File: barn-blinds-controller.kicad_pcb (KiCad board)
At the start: 4 copper layers, 65 x 73.9 mm, 103 parts, among them J1 DC005-T20, J2 USB_B_Micro, J3 Conn_01x05, J4 Phoenix Contact 1786918, SW1 RESET, SW2 BOOT, U1 DCDC Converter, U10 TMP235, U11 ACS723xLCTR-05AB, U12 PRTR5V0U2X, U13 PRTR5V0U2X, U14 PRTR5V0U2X, U15 PRTR5V0U2X, U2 AP2112K-3.3, U3 ESP32-S3-WROOM-1, U4 ISO7760DBQ, U5 ISO7760DBQ, U6 ISO7760DBQ, U7 AMS1117-3.3, U8 TB6612FNG, U9 TB6612FNG

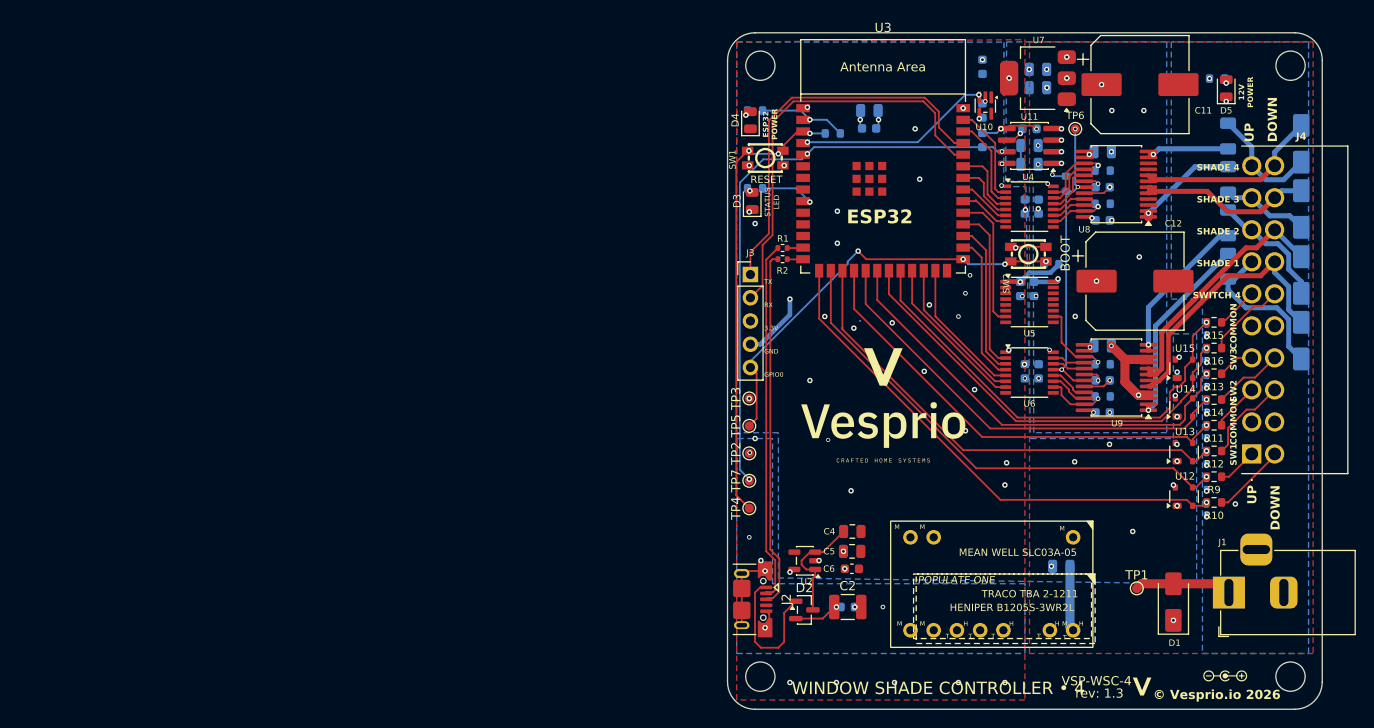
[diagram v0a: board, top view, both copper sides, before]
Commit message: Added RTS/DTS programing via UART circuitry, added LED control circuitry.
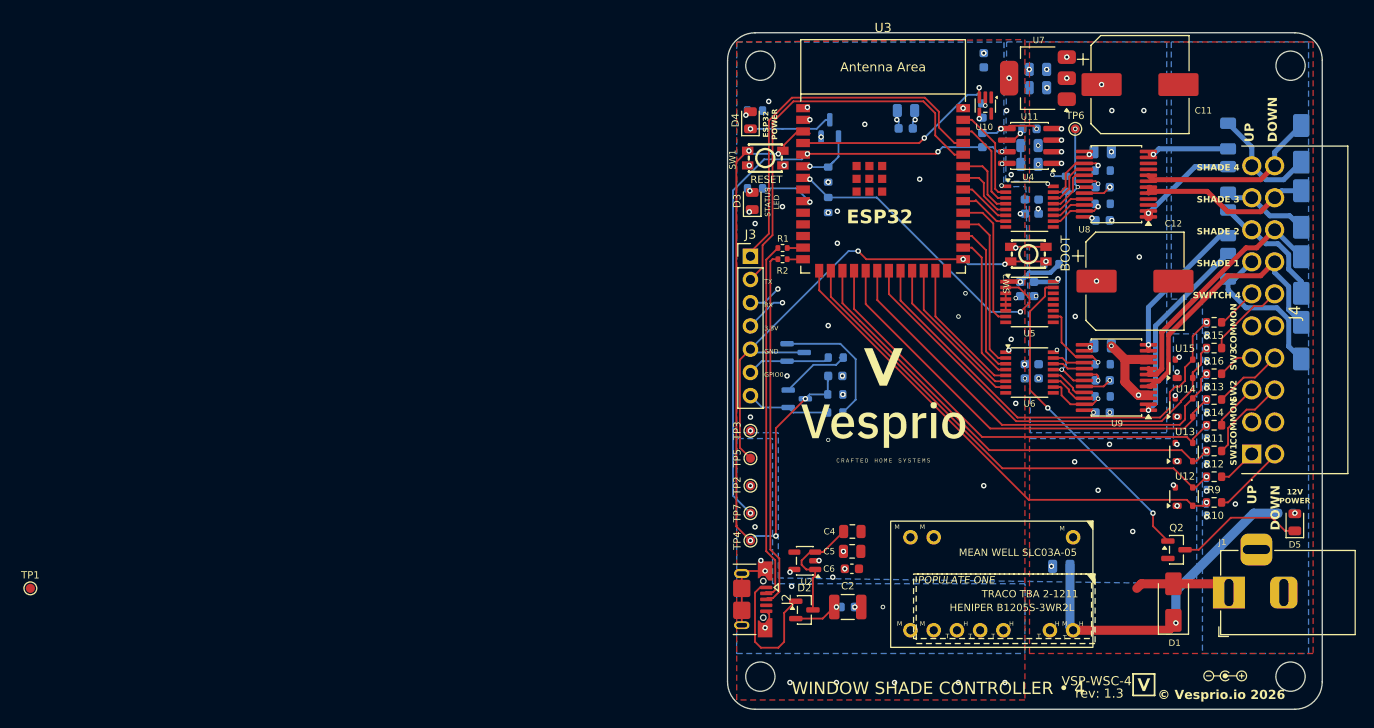
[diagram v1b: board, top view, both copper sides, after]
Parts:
- added C21: 1uF, Capacitor_SMD:C_0603_1608Metric, B.Cu at (88.8, 86.5)
- added Q1: 2N7002, Package_TO_SOT_SMD:SOT-23, B.Cu at (88.2, 59.5)
- added Q2: 2N7002, Package_TO_SOT_SMD:SOT-23, F.Cu at (126.1, 105.5)
- added Q3: S8050, Package_TO_SOT_SMD:SOT-23, B.Cu at (84.4, 83.9)
- added Q4: S8050, Package_TO_SOT_SMD:SOT-23, B.Cu at (84.6, 89.0)
- added R17: 10K, Resistor_SMD:R_0603_1608Metric, B.Cu at (88.0, 67.8)
- added R18: 10K, Resistor_SMD:R_0603_1608Metric, B.Cu at (88.0, 64.5)
- added R19: 10K, Resistor_SMD:R_0603_1608Metric, B.Cu at (88.8, 90.5)
- added R20: 10K, Resistor_SMD:R_0603_1608Metric, B.Cu at (88.8, 84.5)
- J3: value Conn_01x05 -> Conn_01x07; footprint Connector_PinHeader_2.54mm:PinHeader_1x05_P2.54mm_Vertical -> Connector_PinHeader_2.54mm:PinHeader_1x07_P2.54mm_Vertical
- J4: footprint barn_shade_controller:Phoenix Contact 1786918 -> barn_shade_controller:1786918
- U3: footprint Espressif:ESP32-S3-WROOM-1 -> PCM_Espressif:ESP32-S3-WROOM-1
- moved TP1 120.9 mm to (0.80, 109.7)
- moved R_LED3 48.1 mm to (138.0, 101.5)
- moved D5 48.0 mm to (139.0, 102.5)
- moved R3 28.5 mm to (88.8, 88.5)
- moved C7 4.00 mm to (96.5, 59.4)
- moved C8 4.00 mm to (96.5, 57.5)
- moved TP2 3.54 mm to (79.5, 98.5)
- moved TP3 3.54 mm to (79.5, 92.5)
- moved TP4 3.54 mm to (79.5, 104.5)
- moved TP5 3.54 mm to (79.5, 95.5)
- moved TP7 3.54 mm to (79.5, 101.5)
- moved J3 2.00 mm to (79.5, 73.4)
- moved C_TMP1 0.73 mm to (105.0, 52.0)
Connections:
- net Net-(J3-Pin_5) renamed BOOT
- net Net-(U3-EN) renamed EN
- D4 pad 1: GND_ISO -> D4_CATHODE
- D5 pad 1: GND_MOTOR -> D5_CATHODE
- R_LED3 pad 2: +12V -> +12V_RAW
- U3 pad 6: unconnected-(U3-GPIO6/TOUCH6/ADC1_CH5-Pad6) -> LED_D4_EN
- U3 pad 7: unconnected-(U3-GPIO7/TOUCH7/ADC1_CH6-Pad7) -> LED_D5_CTRL
- U5 pad 15: unconnected-(U5-OUTA-Pad15) -> LED_D5_SW
- U5 pad 2: GND_ISO -> LED_D5_CTRL
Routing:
- net LED_D5_SW: track 0.00 -> 35.5 mm, vias 0 -> 2
- net LED_D5_CTRL: track 0.00 -> 34.8 mm, vias 0 -> 2
- net +12V_RAW: track 7.13 -> 36.9 mm
- net EN: track 48.5 -> 74.4 mm, vias 3 -> 5
- net Net-(Q3-B): track 0.00 -> 14.6 mm
- net D5_CATHODE: track 0.00 -> 14.0 mm
- net BOOT: track 44.8 -> 56.0 mm
- net DTR: track 0.00 -> 10.1 mm
- net RTS: track 0.00 -> 9.21 mm
- net D4_CATHODE: track 0.00 -> 9.08 mm, vias 0 -> 1
- net Net-(Q4-B): track 0.00 -> 7.90 mm
- net LED_D4_EN: track 0.00 -> 6.50 mm, vias 0 -> 1
- net +3.3V_ISO: track 18.3 -> 12.7 mm, vias 19 -> 21
- net ACS723: track 63.4 -> 67.7 mm, vias 3 -> 4
- net TMP235: track 20.9 -> 23.1 mm
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
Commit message: Update annotations, fixed font sizes.
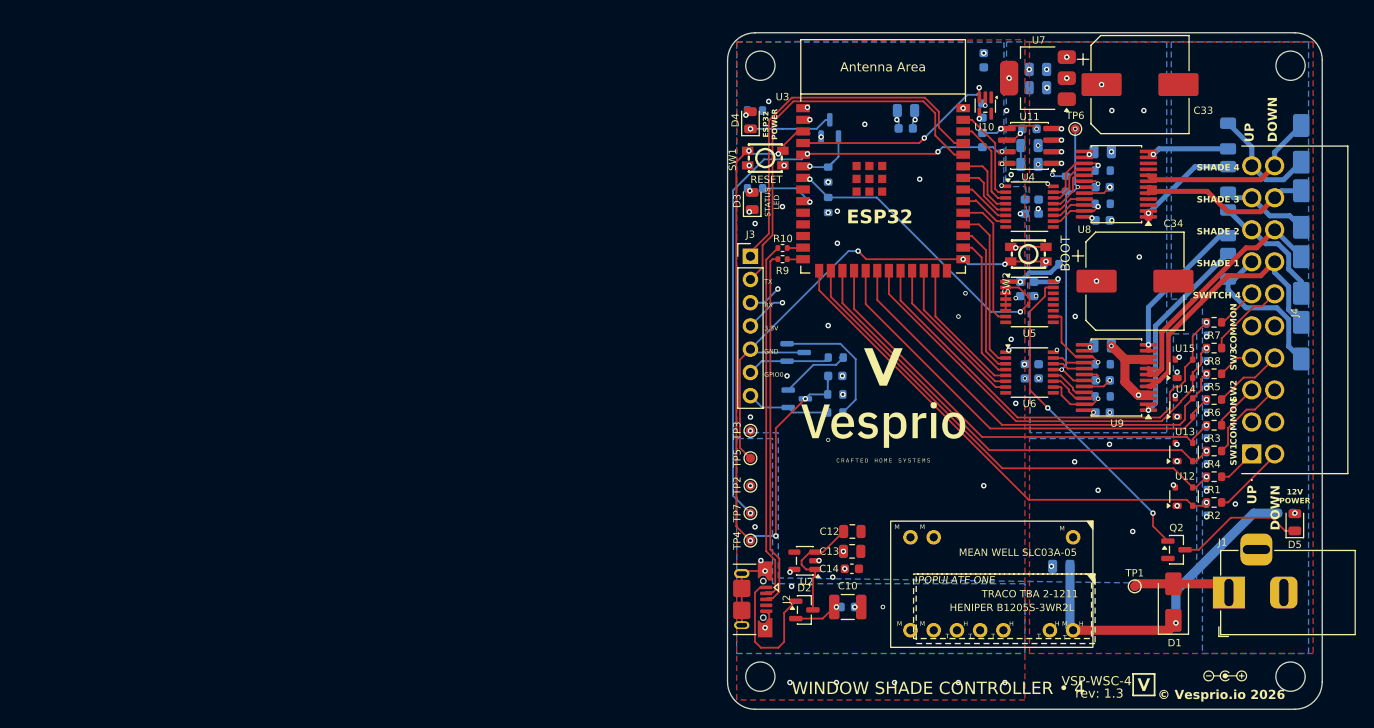
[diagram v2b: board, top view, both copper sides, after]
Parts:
- moved TP1 120.7 mm to (121.5, 109.5)
- renumbered C13 to C1, C2 to C10, C3 to C11, C4 to C12, C5 to C13, C6 to C14, C7 to C15, C8 to C16, C21 to C17, C_ACS1 to C18, C_ACS2 to C19, C14 to C2, C_FILT1 to C20, C_TMP1 to C21, C_ISO_A1 to C22, C_ISO_B1 to C23, C_ISO_C1 to C24, C_ISO_D1 to C25, C_ISO_E1 to C26, C_ISO_F1 to C27, C_VCC_A2 to C28, C_VCC_A1 to C29, C15 to C3, C_VCC_B2 to C30, C_VCC_B1 to C31, C9 to C32, C11 to C33, C12 to C34, C10 to C35, C_VM_A1 to C36, C_VM_A2 to C37, C_VM_B1 to C38, C_VM_B2 to C39, C16 to C4, C17 to C5, C18 to C6, C19 to C7, C20 to C8, C1 to C9, D8 to D7, D9 to D8, D7 to D9, R9 to R1, R1 to R10, R3 to R11, R_BOOT1 to R12, R_LED1 to R13, R_LED2 to R14, R18 to R15, R_LED3 to R16, R19 to R18, R20 to R19, R10 to R2, R7 to R20, R6 to R21, R5 to R22, R4 to R23, R8 to R24, R11 to R3, R12 to R4, R13 to R5, R14 to R6, R15 to R7, R16 to R8, R2 to R9

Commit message: Cleaned up annotations on board.
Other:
- board text added: "COM"
- board text added: "DTR"
- board text added: "RTS"
- board text removed: "COMMON"
